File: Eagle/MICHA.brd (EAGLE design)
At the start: 110.5 x 83.1 mm, 57 parts, among them IC1 LM4041A12LP, K1 PIN20X2, T1 BSS84, U1 ARDUINO_MKR_ZERO, U2 MIKROE_CLICK, X1 RJ45-RJULE4318101, X2 RJ45-RJULE4318101, X3 RJ45-RJULE4318101, X4 RJ45-RJULE4318101, X5 RJ45-RJULE4318101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

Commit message: Speed and power pump pins modified
- Voltage tags on X7
- Output valve names updated
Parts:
- R6, R7: value 2k -> 15-1/4W
- Z1, Z2: value 5,1V/1W -> 5,1V-1W
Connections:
- net VALVE1_CLOSE renamed VALVE1_DIR
- net VALVE1_OPEN renamed VALVE1_POWER
- net VALVE2_CLOSE renamed VALVE2_DIR
- net VALVE2_OPEN renamed VALVE2_POWER
- net D0: now also TBD2.4; no longer TBD2.6
- net D2: now also TBD2.6; no longer TBD2.4
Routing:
- net D2: track 25.2 -> 28.7 mm, vias 0 -> 2
- net D0: track 25.2 -> 23.1 mm, vias 0 -> 2
- net RX_PI: track 64.3 -> 62.8 mm
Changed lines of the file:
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@@
 <attribute name="NAME" x="43.18" y="10.00125" size="1.016" layer="25"/>
 </element>
-<element name="R6" library="resistor" package="R1206" value="2k" x="100.965" y="-4.7625" smashed="yes" rot="R90">
+<element name="R6" library="resistor" package="R1206" value="15-1/4W" x="100.965" y="-4.7625" smashed="yes" rot="R90">
 <attribute name="NAME" x="101.9175" y="-1.11125" size="1.016" layer="25" rot="R180"/>
 </element>
-<element name="R7" library="resistor" package="R1206" value="2k" x="103.505" y="-4.7625" smashed="yes" rot="R90">
+<element name="R7" library="resistor" package="R1206" value="15-1/4W" x="103.505" y="-4.7625" smashed="yes" rot="R90">
 <attribute name="NAME" x="104.4575" y="-1.11125" size="1.016" layer="25" rot="R180"/>
 </element>
@@
 <attribute name="NAME" x="20.8026" y="35.4203" size="1.016" layer="25"/>
 </element>
-<element name="Z1" library="Zener_SMA" package="ZENER_SMA" value="5,1V/1W" x="95.5675" y="-6.6675" smashed="yes" rot="R180">
+<element name="Z1" library="Zener_SMA" package="ZENER_SMA" value="5,1V-1W" x="95.5675" y="-6.6675" smashed="yes" rot="R180">
 <attribute name="NAME" x="99.2505" y="-4.953" size="1.016" layer="25" rot="R180"/>
 </element>
-<element name="Z2" library="Zener_SMA" package="ZENER_SMA" value="5,1V/1W" x="88.5825" y="-6.6675" smashed="yes">
+<element name="Z2" library="Zener_SMA" package="ZENER_SMA" value="5,1V-1W" x="88.5825" y="-6.6675" smashed="yes">
 <attribute name="NAME" x="90.6145" y="-5.921375" size="1.016" layer="25"/>
 </element>
@@
 <wire x1="79.6925" y1="15.24" x2="79.6925" y2="13.6525" width="0.1524" layer="1"/>
 <wire x1="79.6925" y1="13.6525" x2="79.0575" y2="13.0175" width="0.1524" layer="1"/>
-<wire x1="79.0575" y1="13.0175" x2="72.39" y2="13.0175" width="0.1524" layer="1"/>
-<wire x1="72.39" y1="13.0175" x2="66.04" y2="19.3675" width="0.1524" layer="1"/>
-<wire x1="66.04" y1="19.3675" x2="42.8625" y2="19.3675" width="0.1524" layer="1"/>
+<wire x1="79.0575" y1="13.0175" x2="70.485" y2="13.0175" width="0.1524" layer="1"/>
+<wire x1="70.485" y1="13.0175" x2="64.135" y2="19.3675" width="0.1524" layer="1"/>
+<wire x1="64.135" y1="19.3675" x2="42.8625" y2="19.3675" width="0.1524" layer="1"/>
 <wire x1="42.8625" y1="19.3675" x2="42.062" y2="18.567" width="0.1524" layer="1"/>
 <wire x1="42.062" y1="18.567" x2="42.062" y2="10.4775" width="0.1524" layer="1"/>
@@
 <wire x1="91.44" y1="46.0375" x2="93.345" y2="46.0375" width="0.1524" layer="1"/>
 </signal>
-<signal name="VALVE1_OPEN">
+<signal name="VALVE1_POWER">
 <contactref element="X2" pad="2"/>
 <contactref element="TBD1" pad="16"/>
@@
 <wire x1="92.23375" y1="22.38375" x2="93.345" y2="22.38375" width="0.4064" layer="16"/>
 </signal>
-<signal name="VALVE1_CLOSE">
+<signal name="VALVE1_DIR">
 <contactref element="X2" pad="1"/>
 <contactref element="TBD1" pad="15"/>
@@
 <wire x1="95.885" y1="21.11375" x2="95.72625" y2="20.955" width="0.4064" layer="16"/>
 </signal>
-<signal name="VALVE2_OPEN">
+<signal name="VALVE2_POWER">
 <contactref element="TBD2" pad="18"/>
 <wire x1="90.2486" y1="24.5261" x2="87.63" y2="21.9075" width="0.4064" layer="1"/>
@@
 <wire x1="91.9057625" y1="30.00375" x2="93.345" y2="30.00375" width="0.4064" layer="1"/>
 </signal>
-<signal name="VALVE2_CLOSE">
+<signal name="VALVE2_DIR">
 <contactref element="TBD2" pad="17"/>
 <wire x1="85.725" y1="19.3675" x2="86.36" y2="19.3675" width="0.4064" layer="1"/>
@@
 <signal name="D0">
 <contactref element="U1" pad="J4_9"/>
-<contactref element="TBD2" pad="6"/>
-<wire x1="78.105" y1="9.2075" x2="74.295" y2="9.2075" width="0.1524" layer="1"/>
-<wire x1="74.295" y1="9.2075" x2="67.9877" y2="15.5148" width="0.1524" layer="1"/>
-<wire x1="67.9877" y1="15.5148" x2="55.5625" y2="15.5148" width="0.1524" layer="1"/>
+<wire x1="66.0827" y1="15.5148" x2="55.5625" y2="15.5148" width="0.1524" layer="1"/>
+<contactref element="TBD2" pad="4"/>
+<via x="66.0827" y="15.5148" extent="1-16" drill="0.35"/>
+<wire x1="66.0827" y1="15.5148" x2="66.1254" y2="15.5575" width="0.1524" layer="16"/>
+<wire x1="66.1254" y1="15.5575" x2="69.85" y2="15.5575" width="0.1524" layer="16"/>
+<via x="69.85" y="15.5575" extent="1-16" drill="0.35"/>
+<wire x1="69.85" y1="15.5575" x2="70.00875" y2="15.5575" width="0.1524" layer="1"/>
+<wire x1="70.00875" y1="15.5575" x2="71.27875" y2="14.2875" width="0.1524" layer="1"/>
+<wire x1="71.27875" y1="14.2875" x2="78.105" y2="14.2875" width="0.1524" layer="1"/>
 </signal>
 <signal name="D1">
 <contactref element="U1" pad="J4_10"/>
 <contactref element="TBD2" pad="5"/>
-<wire x1="78.105" y1="11.7475" x2="72.7075" y2="11.7475" width="0.1524" layer="1"/>
-<wire x1="72.7075" y1="11.7475" x2="66.4002" y2="18.0548" width="0.1524" layer="1"/>
-<wire x1="66.4002" y1="18.0548" x2="55.5625" y2="18.0548" width="0.1524" layer="1"/>
+<wire x1="78.105" y1="11.7475" x2="70.8025" y2="11.7475" width="0.1524" layer="1"/>
+<wire x1="70.8025" y1="11.7475" x2="64.4952" y2="18.0548" width="0.1524" layer="1"/>
+<wire x1="64.4952" y1="18.0548" x2="55.5625" y2="18.0548" width="0.1524" layer="1"/>
 </signal>
 <signal name="D2">
 <contactref element="U1" pad="J4_11"/>
-<contactref element="TBD2" pad="4"/>
-<wire x1="78.105" y1="14.2875" x2="72.0725" y2="14.2875" width="0.1524" layer="1"/>
-<wire x1="72.0725" y1="14.2875" x2="65.7652" y2="20.5948" width="0.1524" layer="1"/>
-<wire x1="65.7652" y1="20.5948" x2="55.5625" y2="20.5948" width="0.1524" layer="1"/>
+<wire x1="55.5625" y1="20.5948" x2="63.8602" y2="20.5948" width="0.1524" layer="1"/>
+<contactref element="TBD2" pad="6"/>
+<via x="70.8025" y="13.6525" extent="1-16" drill="0.35"/>
+<wire x1="70.8025" y1="13.6525" x2="70.8025" y2="11.1125" width="0.1524" layer="16"/>
+<via x="70.8025" y="11.1125" extent="1-16" drill="0.35"/>
+<wire x1="70.8025" y1="11.1125" x2="71.4375" y2="10.4775" width="0.1524" layer="1"/>
+<wire x1="76.835" y1="10.4775" x2="78.105" y2="9.2075" width="0.1524" layer="1"/>
+<wire x1="63.8602" y1="20.5948" x2="70.8025" y2="13.6525" width="0.1524" layer="1"/>
+<wire x1="71.4375" y1="10.4775" x2="76.835" y2="10.4775" width="0.1524" layer="1"/>
 </signal>
 <signal name="PUMP_PAUSE_LED">
@@
 <contactref element="U1" pad="J5_5"/>
 <contactref element="TBD2" pad="2"/>
-<wire x1="78.105" y1="19.3675" x2="67.9027625" y2="19.3675" width="0.1524" layer="1"/>
-<wire x1="67.9027625" y1="19.3675" x2="65.6017125" y2="21.66855" width="0.1524" layer="1"/>
-<wire x1="65.6017125" y1="21.66855" x2="38.85625" y2="21.66855" width="0.1524" layer="1"/>
+<wire x1="78.105" y1="19.3675" x2="65.9977625" y2="19.3675" width="0.1524" layer="1"/>
+<wire x1="65.9977625" y1="19.3675" x2="63.6967125" y2="21.66855" width="0.1524" layer="1"/>
+<wire x1="63.6967125" y1="21.66855" x2="38.85625" y2="21.66855" width="0.1524" layer="1"/>
 <wire x1="38.85625" y1="21.66855" x2="35.2425" y2="18.0548" width="0.1524" layer="1"/>
 </signal>
@@
 <wire x1="44.1325" y1="8.89" x2="44.1325" y2="17.9324" width="0.1524" layer="1"/>
 <via x="44.1325" y="17.9324" extent="1-16" drill="0.35"/>
-<wire x1="45.9273375" y1="28.2089125" x2="45.9273375" y2="19.7272375" width="0.1524" layer="16"/>
-<wire x1="44.1325" y1="17.9324" x2="45.9273375" y2="19.7272375" width="0.1524" layer="16"/>
-<wire x1="45.9273375" y1="28.2089125" x2="24.92375" y2="49.2125" width="0.1524" layer="16"/>
-<wire x1="24.92375" y1="49.2125" x2="18.5251625" y2="49.2125" width="0.1524" layer="16"/>
+<wire x1="18.5251625" y1="49.2125" x2="24.92375" y2="49.2125" width="0.1524" layer="16"/>
 <wire x1="17.2974" y1="50.4402625" x2="17.2974" y2="52.89235" width="0.1524" layer="16"/>
 <wire x1="18.38" y1="53.74" x2="18.14505" y2="53.74" width="0.1524" layer="16"/>
 <wire x1="18.14505" y1="53.74" x2="17.2974" y2="52.89235" width="0.1524" layer="16"/>
 <wire x1="18.5251625" y1="49.2125" x2="17.2974" y2="50.4402625" width="0.1524" layer="16"/>
+<wire x1="44.1325" y1="30.00375" x2="44.1325" y2="17.9324" width="0.1524" layer="16"/>
+<wire x1="24.92375" y1="49.2125" x2="44.1325" y2="30.00375" width="0.1524" layer="16"/>
 </signal>
 <signal name="PI18">

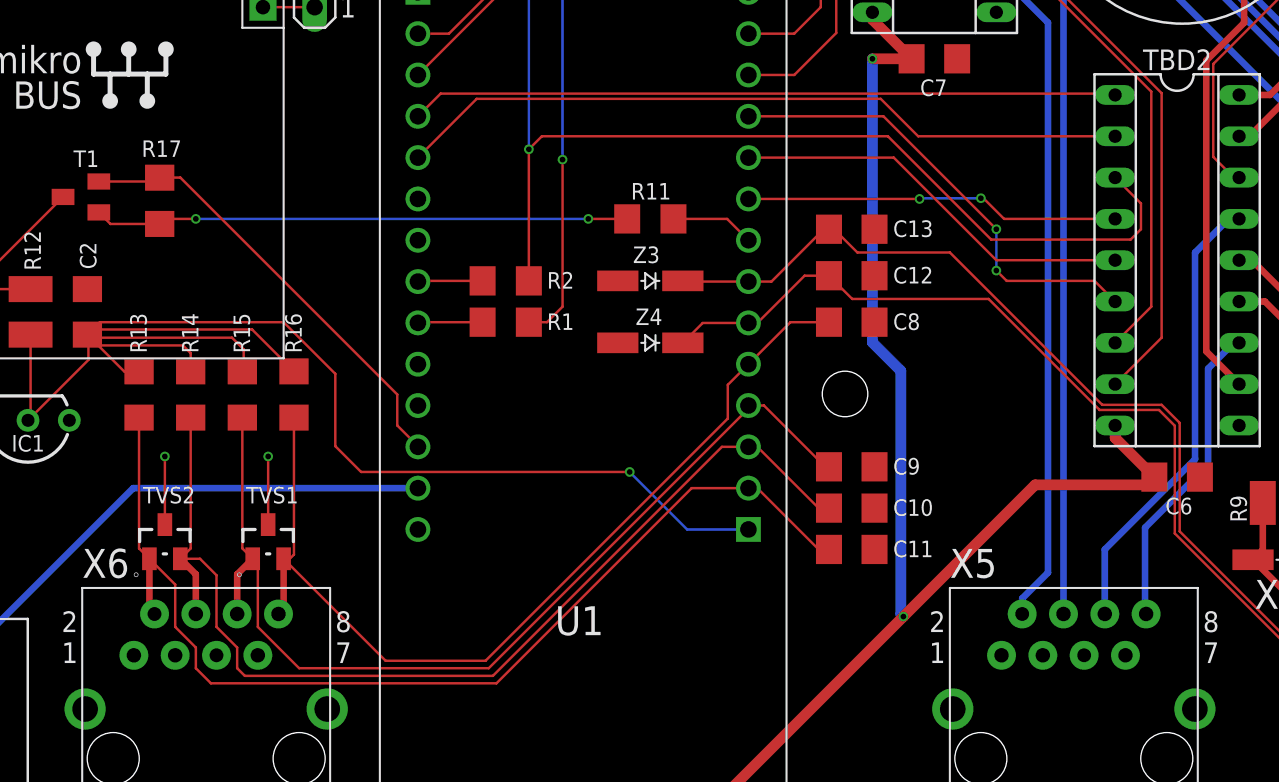
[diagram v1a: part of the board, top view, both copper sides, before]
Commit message: Pump servo pin updated
Modification of the next pins:
- Thermis power -> A0
- Error pump -> A1
- Servo pin -> A2
- Thermi 1 -> A3
- Thermi 2 -> A4
- Thermi 3 -> A5
- Thermi 4 -> A6
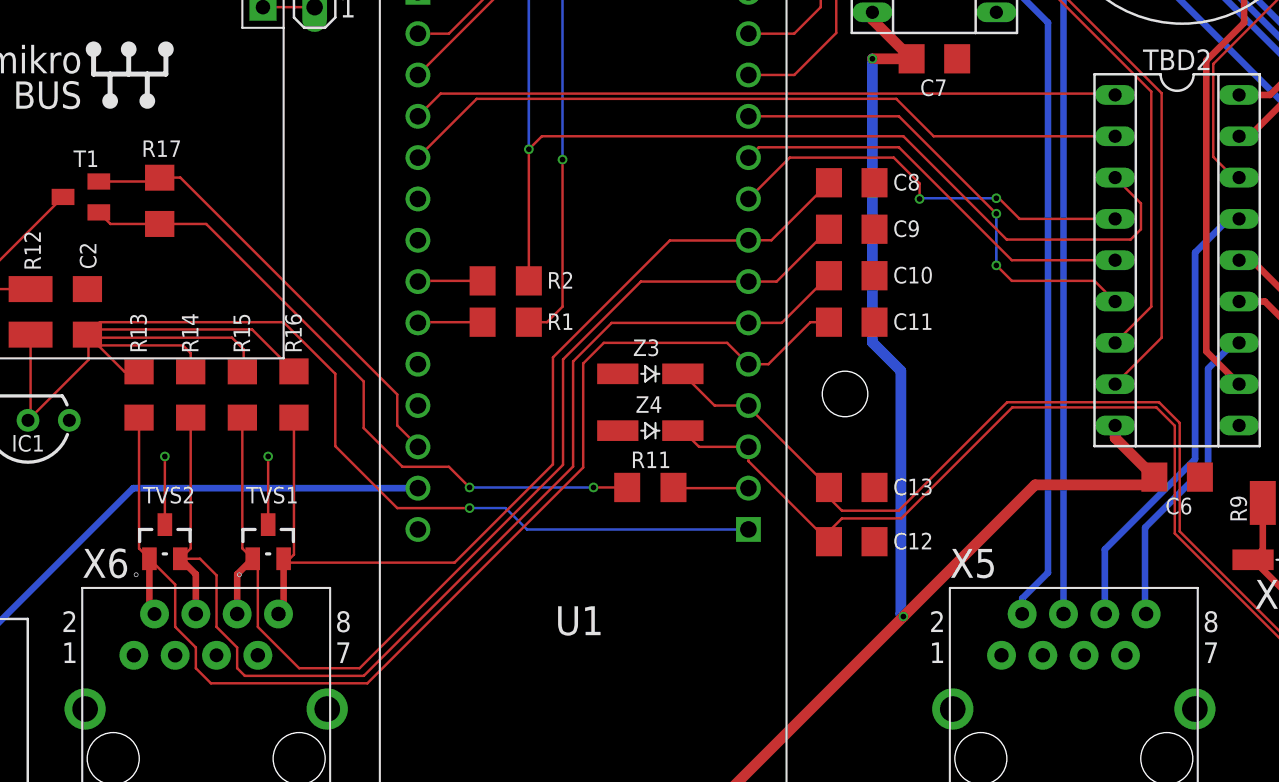
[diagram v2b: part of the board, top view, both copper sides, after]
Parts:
- moved R11 16.5 mm to (49.5, -2.22)
- moved C12 16.4 mm to (61.9, -5.56)
- moved C13 15.9 mm to (61.9, -2.22)
- moved C9 14.6 mm to (61.9, 13.7)
- moved C10 14.3 mm to (61.9, 10.8)
- moved C11 14.0 mm to (61.9, 7.94)
- moved C8 8.57 mm to (61.9, 16.5)
- moved Z3 5.71 mm to (49.5, 4.76)
- moved Z4 5.40 mm to (49.5, 1.27)
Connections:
- net SOL_WARM renamed SOL_HOT
- net D19: now also U1.J4_3; no longer U1.J4_6
- net D21: now also U1.J4_2; no longer U1.J4_8
- net N$14: now also U1.J4_4; no longer U1.J4_7
- net THERMI1: now also U1.J4_5; no longer U1.J4_2
- net THERMI2: now also U1.J4_6; no longer U1.J4_3
- net THERMI3: now also U1.J4_7; no longer U1.J4_4
- net THERMI4: now also U1.J4_8; no longer U1.J4_5
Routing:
- net N$3: track 32.9 -> 41.2 mm
- net THERMI1: track 66.2 -> 73.7 mm
- net THERMI3: track 61.6 -> 68.2 mm
- net THERMI2: track 65.6 -> 72.2 mm
- net D0: track 23.1 -> 25.7 mm
- net D19: track 87.2 -> 88.9 mm
- net THERMI4: track 58.5 -> 59.7 mm
- net N$14: track 86.9 -> 87.9 mm
- net D1: track 25.2 -> 25.7 mm
- net D21: track 5.15 -> 4.63 mm

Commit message: Downgrade to current version of PCB
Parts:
- R6, R7: value 15-1/4W -> 2k
- Z1, Z2: value 5,1V-1W -> 5,1V/1W
- moved R11 16.5 mm to (49.5, 14.3)
- moved C12 16.4 mm to (61.9, 10.8)
- moved C13 15.9 mm to (61.9, 13.7)
- moved C9 14.6 mm to (61.9, -0.95)
- moved C10 14.3 mm to (61.9, -3.49)
- moved C11 14.0 mm to (61.9, -6.03)
- moved C8 8.57 mm to (61.9, 7.94)
- moved Z3 5.71 mm to (49.5, 10.5)
- moved Z4 5.40 mm to (49.5, 6.67)
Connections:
- net SOL_HOT renamed SOL_WARM
- net VALVE1_DIR renamed VALVE1_CLOSE
- net VALVE1_POWER renamed VALVE1_OPEN
- net VALVE2_DIR renamed VALVE2_CLOSE
- net VALVE2_POWER renamed VALVE2_OPEN
- net D0: now also TBD2.6; no longer TBD2.4
- net D19: now also U1.J4_6; no longer U1.J4_3
- net D2: now also TBD2.4; no longer TBD2.6
- net D21: now also U1.J4_8; no longer U1.J4_2
- net N$14: now also U1.J4_7; no longer U1.J4_4
- net THERMI1: now also U1.J4_2; no longer U1.J4_5
- net THERMI2: now also U1.J4_3; no longer U1.J4_6
- net THERMI3: now also U1.J4_4; no longer U1.J4_7
- net THERMI4: now also U1.J4_5; no longer U1.J4_8
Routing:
- net N$3: track 41.2 -> 32.9 mm
- net THERMI1: track 73.7 -> 66.2 mm
- net THERMI3: track 68.2 -> 61.6 mm
- net THERMI2: track 72.2 -> 65.6 mm
- net D2: track 29.1 -> 25.2 mm, vias 2 -> 0
- net D19: track 88.9 -> 87.2 mm
- net RX_PI: track 62.8 -> 64.3 mm
- net THERMI4: track 59.7 -> 58.5 mm
- net N$14: track 87.9 -> 86.9 mm
- net D0: track 25.7 -> 25.2 mm, vias 2 -> 0
- net D1: track 25.7 -> 25.2 mm
- net D21: track 4.63 -> 5.15 mm
